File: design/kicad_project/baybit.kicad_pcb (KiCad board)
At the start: 4 copper layers, 42 x 85 mm, 108 parts, among them J1 EXT_PWR DNI, J2 USB_B_Micro, J3 ER-TFT1.44-1, J4 EXT_LED DNI, J5 U_FL DNI, J6 MIKROBUS_HOST_CONN 8+8P, Q1 BSD235C, Q2 BC847BS, Q3 BC848, SW1 B3U-1000P, SW2 ALPS_SKRH, SW3 RS282G05A3, SW4 RS282G05A3, U1 TPD2EUSB30A, U2 CP2102N-Axx-GQFN28, U3 XC6220B331MR, U4 WS2811, U5 LSM303AGR, U6 ESP32-PICO-D4, U7 PCF8574-SO16, U8 TSC2007IPW

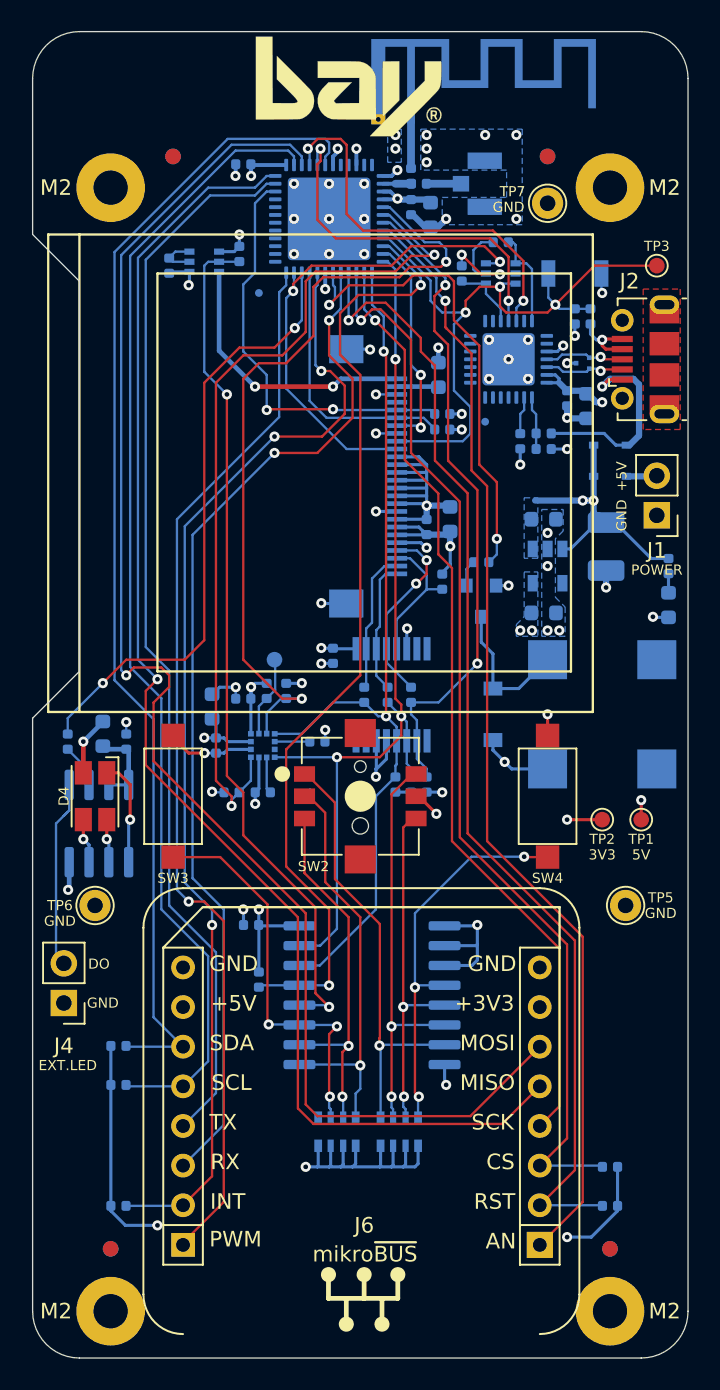
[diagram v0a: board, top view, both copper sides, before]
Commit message: Migrated to Kicad 6
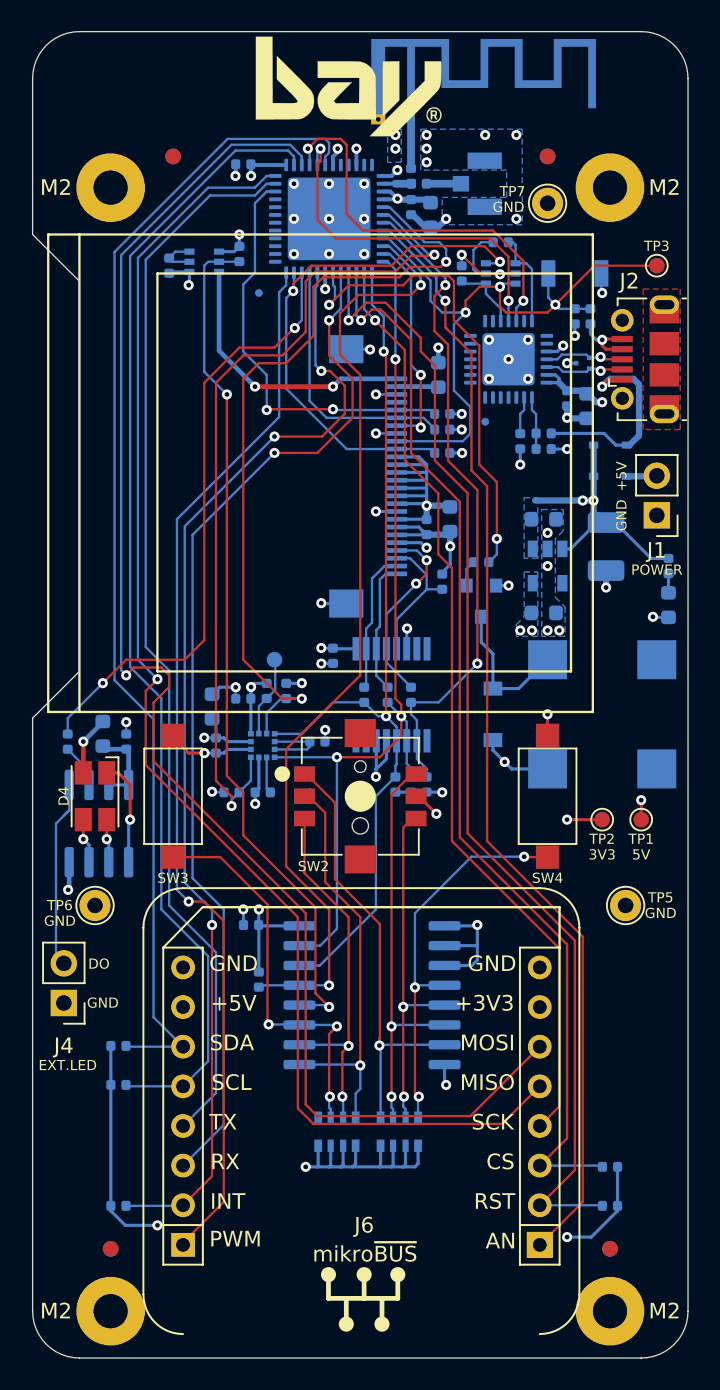
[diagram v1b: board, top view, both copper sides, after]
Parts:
- added R35: 10k, Resistor_SMD:R_0402_1005Metric, B.Cu at (181.2, 72.0)
- BZ1: value G8503C -> SMT-8540C
- C9: value 100n -> 1u
- R11: value 10k -> 10k DNI
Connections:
- U5 pad 3: Net-(U5-Pad3) -> Net-(R13-Pad1)
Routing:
- net Net-(R13-Pad1): track 2.27 -> 4.92 mm
- net TFT_MOSI: track 32.4 -> 34.9 mm
- net +3V3: track 100.4 -> 101.2 mm, vias 28 -> 29
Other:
- net class Default removed
- net class Power removed
- board text added: "200316"
- board text added: "Rev:A1"
- board text removed: "200115"
- board text removed: "Rev:A0"

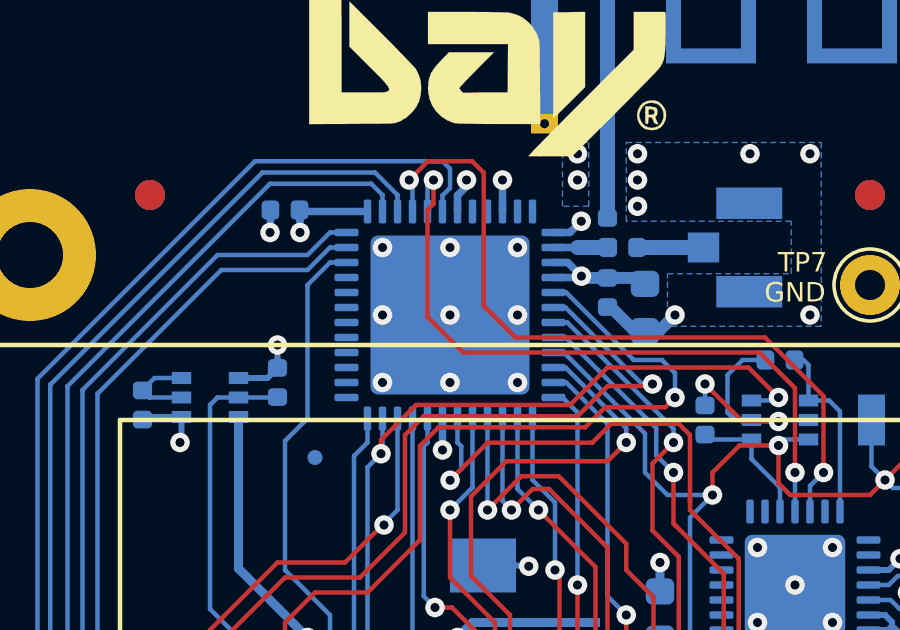
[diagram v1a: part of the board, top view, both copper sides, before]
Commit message: Migrated to Kicad 9
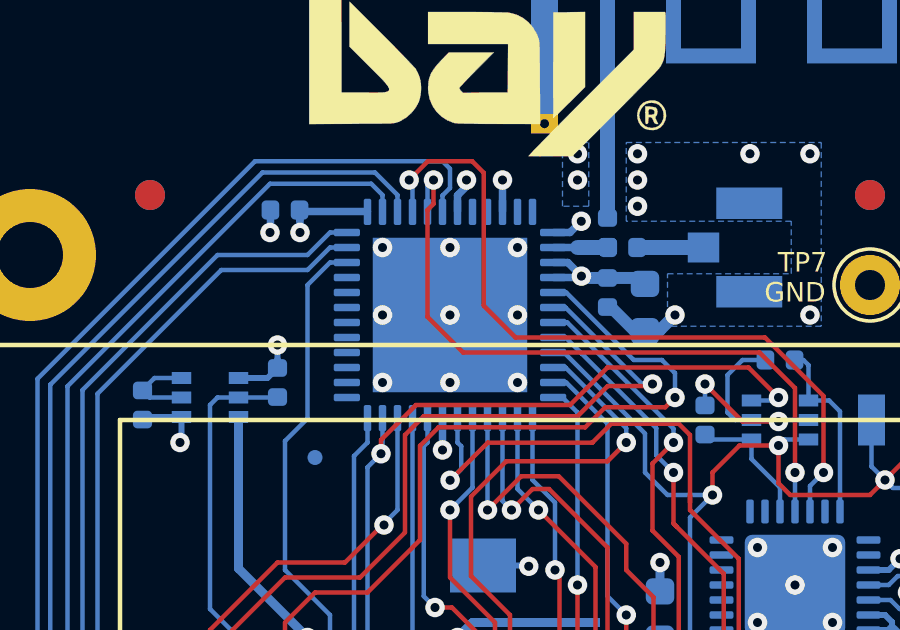
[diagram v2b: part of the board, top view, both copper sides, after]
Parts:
- U6: footprint Package_DFN_QFN:QFN-48-1EP_7x7mm_P0.5mm_EP5.3x5.3mm -> Package_DFN_QFN:QFN-48-1EP_7x7mm_P0.5mm_EP5.15x5.15mm
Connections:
- J3 pad 4: Net-(J3-Pad4) -> unconnected-(J3-TE-Pad4)
- RN2 pad 1: Net-(RN2-Pad1) -> unconnected-(RN2-R1.1-Pad1)
- U2 pad 1: Net-(U2-Pad1) -> unconnected-(U2-~{DCD}-Pad1)
- U2 pad 10: Net-(U2-Pad10) -> unconnected-(U2-NC-Pad10)
- U2 pad 11: Net-(U2-Pad11) -> unconnected-(U2-~{SUSPENDb}-Pad11)
- U2 pad 12: Net-(U2-Pad12) -> unconnected-(U2-SUSPEND-Pad12)
- U2 pad 13: Net-(U2-Pad13) -> unconnected-(U2-CHREN-Pad13)
- U2 pad 14: Net-(U2-Pad14) -> unconnected-(U2-CHR1-Pad14)
- U2 pad 15: Net-(U2-Pad15) -> unconnected-(U2-CHR0-Pad15)
- U2 pad 16: Net-(U2-Pad16) -> unconnected-(U2-~{WAKEUP}/GPIO.3-Pad16)
- U2 pad 17: Net-(U2-Pad17) -> unconnected-(U2-RS485/GPIO.2-Pad17)
- U2 pad 18: Net-(U2-Pad18) -> unconnected-(U2-~{RXT}/GPIO.1-Pad18)
- U2 pad 19: Net-(U2-Pad19) -> unconnected-(U2-~{TXT}/GPIO.0-Pad19)
- U2 pad 2: Net-(U2-Pad2) -> unconnected-(U2-~{RI}/CLK-Pad2)
- U2 pad 20: Net-(U2-Pad20) -> unconnected-(U2-GPIO.6-Pad20)
- U2 pad 21: Net-(U2-Pad21) -> unconnected-(U2-GPIO.5-Pad21)
- U2 pad 22: Net-(U2-Pad22) -> unconnected-(U2-GPIO.4-Pad22)
- U2 pad 23: Net-(U2-Pad23) -> unconnected-(U2-~{CTS}-Pad23)
- U2 pad 27: Net-(U2-Pad27) -> unconnected-(U2-~{DSR}-Pad27)
- U3 pad 4: Net-(U3-Pad4) -> unconnected-(U3-NC-Pad4)
- U6 pad 25: Net-(U6-Pad25) -> unconnected-(U6-IO16-Pad25)
- U6 pad 26: Net-(U6-Pad26) -> unconnected-(U6-VDD_SDIO-Pad26)
- U6 pad 27: Net-(U6-Pad27) -> unconnected-(U6-IO17-Pad27)
- U6 pad 28: Net-(U6-Pad28) -> unconnected-(U6-SD2/IO9-Pad28)
- U6 pad 29: Net-(U6-Pad29) -> unconnected-(U6-SD3/IO10-Pad29)
- U6 pad 30: Net-(U6-Pad30) -> unconnected-(U6-CMD-Pad30)
- U6 pad 31: Net-(U6-Pad31) -> unconnected-(U6-CLK-Pad31)
- U6 pad 32: Net-(U6-Pad32) -> unconnected-(U6-SD0-Pad32)
- U6 pad 33: Net-(U6-Pad33) -> unconnected-(U6-SD1-Pad33)
- U6 pad 44: Net-(U6-Pad44) -> unconnected-(U6-XTAL_N_NC-Pad44)
- U6 pad 45: Net-(U6-Pad45) -> unconnected-(U6-XTAL_P_NC-Pad45)
- U6 pad 47: Net-(U6-Pad47) -> unconnected-(U6-CAP2_NC-Pad47)
- U6 pad 48: Net-(U6-Pad48) -> unconnected-(U6-CAP1_NC-Pad48)
- U8 pad 16: Net-(U8-Pad16) -> unconnected-(U8-AUX-Pad16)
